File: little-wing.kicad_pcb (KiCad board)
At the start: 2 copper layers, 119.8 x 95.1 mm, 72 parts, among them IC1 AP7335-WG-7, J1 nice!view, J2 Battery, J3 trackball, J4 trackball, SW1 Power, SW2 Reset, U1 nice!nano v2, U2 PMW3610

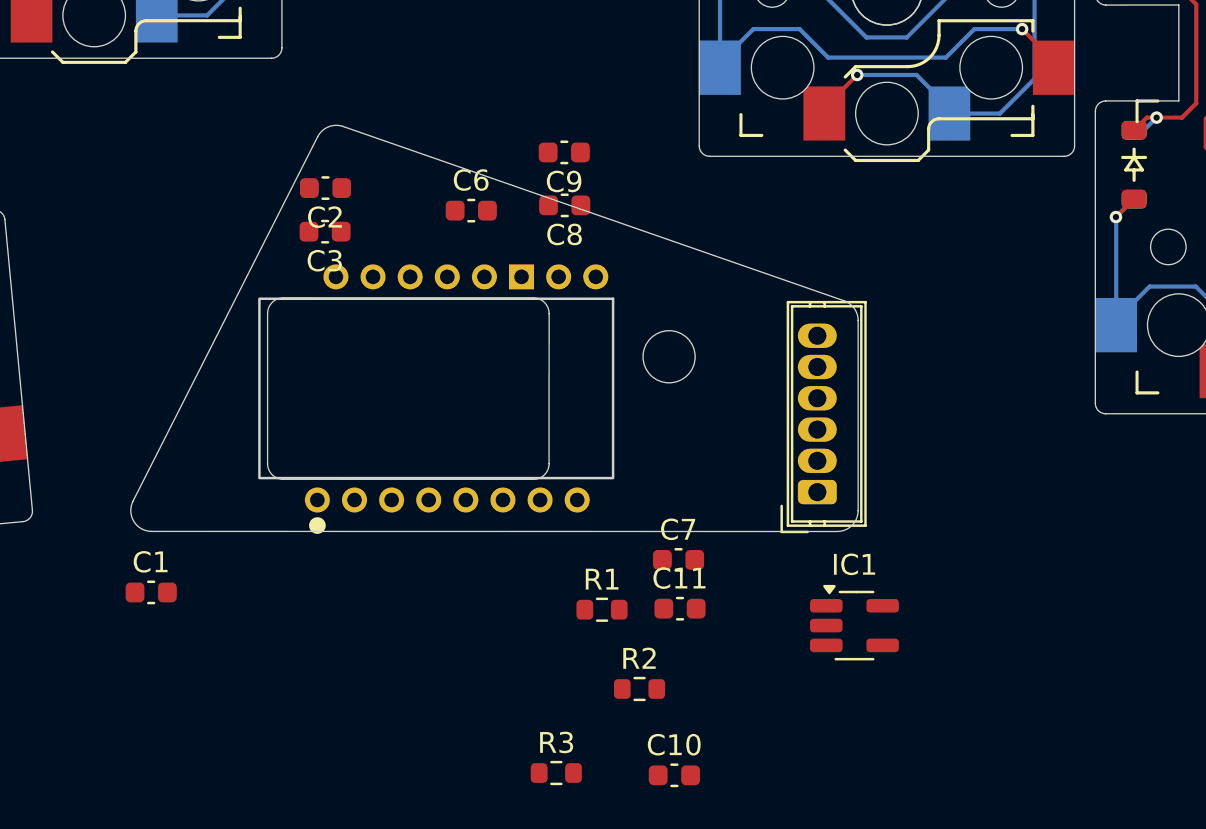
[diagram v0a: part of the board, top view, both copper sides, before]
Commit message: Initial alignment of the sensor block
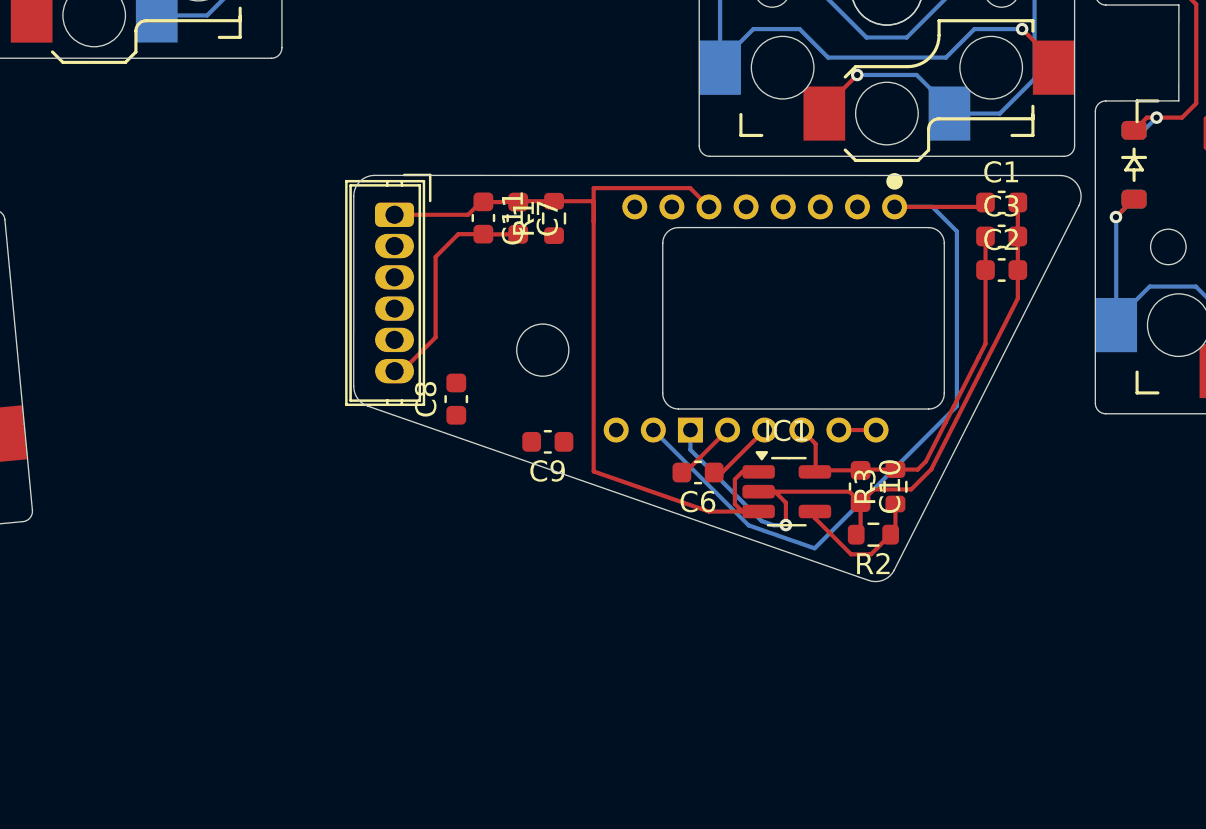
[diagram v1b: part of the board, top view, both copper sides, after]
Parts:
- moved C1 44.9 mm to (188.5, 124.5)
- moved C2 32.7 mm to (188.5, 127.7), turned to 0 degrees
- moved C3 32.4 mm to (188.5, 126.1), turned to 0 degrees
- moved J3 24.2 mm to (159.4, 125.1), turned to -90 degrees
- moved R3 21.3 mm to (183.4, 138.1), turned to 90 degrees
- moved C11 21.0 mm to (163.6, 125.2), turned to -90 degrees
- moved U2 19.4 mm to (179.1, 130.1), turned to -90 degrees
- moved R1 18.9 mm to (167.0, 125.3), turned to 90 degrees
- moved C7 18.1 mm to (165.3, 125.3), turned to -90 degrees
- moved C6 16.6 mm to (173.9, 137.4), turned to 180 degrees
- moved C10 16.5 mm to (181.7, 138.1), turned to -90 degrees
- moved C9 13.9 mm to (166.7, 136.0)
- moved R2 13.4 mm to (182.3, 140.4), turned to 180 degrees
- moved C8 10.6 mm to (162.3, 133.9), turned to 90 degrees
- moved IC1 7.19 mm to (178.2, 138.4)
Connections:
- D1 pad 1: Row 0 -> Row 2
- D10 pad 1: Row 0 -> Row 2
- D12 pad 1: Row 2 -> Row 0
- D13 pad 1: Row 0 -> Row 2
- D15 pad 1: Row 2 -> Row 0
- D16 pad 1: Row 0 -> Row 2
- D3 pad 1: Row 2 -> Row 0
- D4 pad 1: Row 0 -> Row 2
- D6 pad 1: Row 2 -> Row 0
- D7 pad 1: Row 0 -> Row 2
- D9 pad 1: Row 2 -> Row 0
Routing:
- net Row 2: track 398.2 -> 165.3 mm, vias 26 -> 6
- net Row 0: track 165.3 -> 398.2 mm, vias 6 -> 26
- net GND: track 504.3 -> 549.9 mm, vias 15 -> 16
- net 3.3v: track 0.00 -> 42.3 mm
- net Net-(U2-+VCSEL): track 0.00 -> 35.8 mm
- net +1V9: track 0.00 -> 19.7 mm
- net Net-(IC1-ADJ): track 0.00 -> 6.62 mm
- net Net-(U2-CN): track 0.00 -> 3.26 mm
- net Net-(U2-CP): track 0.00 -> 3.03 mm
- net Net-(U2--VCSEL): track 0.00 -> 1.78 mm
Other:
- outline, holes or cut-outs redrawn

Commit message: Wiring togother the sensor board
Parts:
- moved C1 40.6 mm to (150.5, 139.0), turned to 180 degrees
- moved C3 39.6 mm to (150.5, 137.3), turned to 180 degrees
- moved C2 38.8 mm to (150.5, 135.7), turned to 180 degrees
- moved R2 30.8 mm to (156.9, 123.0), turned to 0 degrees
- moved R3 30.6 mm to (155.6, 125.3), turned to -90 degrees
- moved C10 27.6 mm to (157.3, 125.4), turned to 90 degrees
- moved J3 24.2 mm to (179.5, 138.4), turned to 90 degrees
- moved IC1 21.8 mm to (160.8, 125.1), turned to 180 degrees
- moved U2 19.4 mm to (159.9, 133.4), turned to 90 degrees
- moved C11 17.5 mm to (175.4, 138.2), turned to 90 degrees
- moved C7 15.5 mm to (173.7, 138.2), turned to 90 degrees
- moved C8 14.8 mm to (176.9, 136.4), turned to -90 degrees
- moved C6 14.4 mm to (165.1, 126.0), turned to 0 degrees
- moved R1 13.9 mm to (172.0, 138.2), turned to -90 degrees
- moved C9 10.6 mm to (176.9, 133.3), turned to 90 degrees
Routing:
- net SCLK: track 0.00 -> 53.9 mm, vias 0 -> 2
- net SDIO: track 0.00 -> 53.3 mm
- net NCS: track 0.00 -> 18.3 mm
- net GND: track 549.9 -> 566.8 mm
- net Net-(U2-VCP): track 0.48 -> 15.9 mm
- net MOTION: track 0.00 -> 15.1 mm
- net Net-(U2-NRESET): track 0.00 -> 6.21 mm
- net Net-(U2-+VCSEL): track 35.8 -> 31.9 mm
- net 3.3v: track 42.3 -> 41.4 mm, vias 0 -> 4
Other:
- outline, holes or cut-outs redrawn

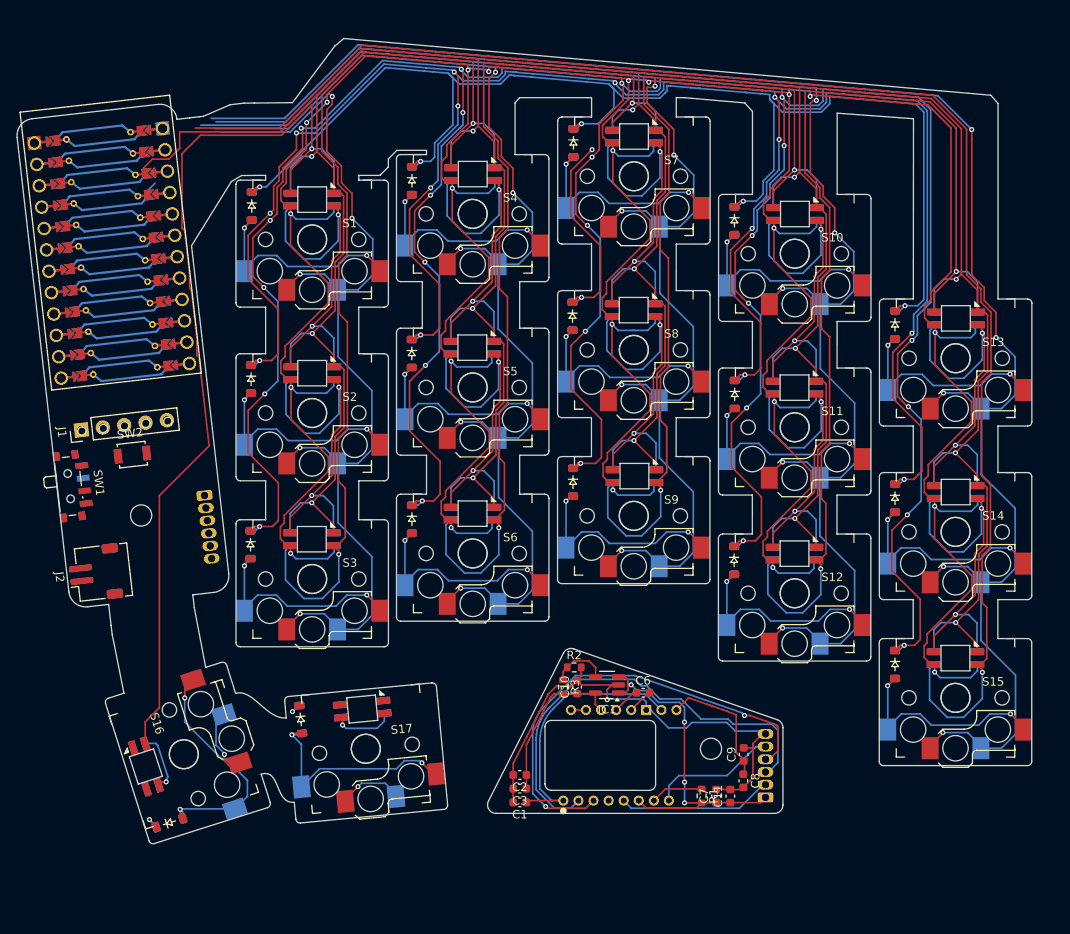
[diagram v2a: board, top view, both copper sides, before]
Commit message: Rounding out the main columns cutouts
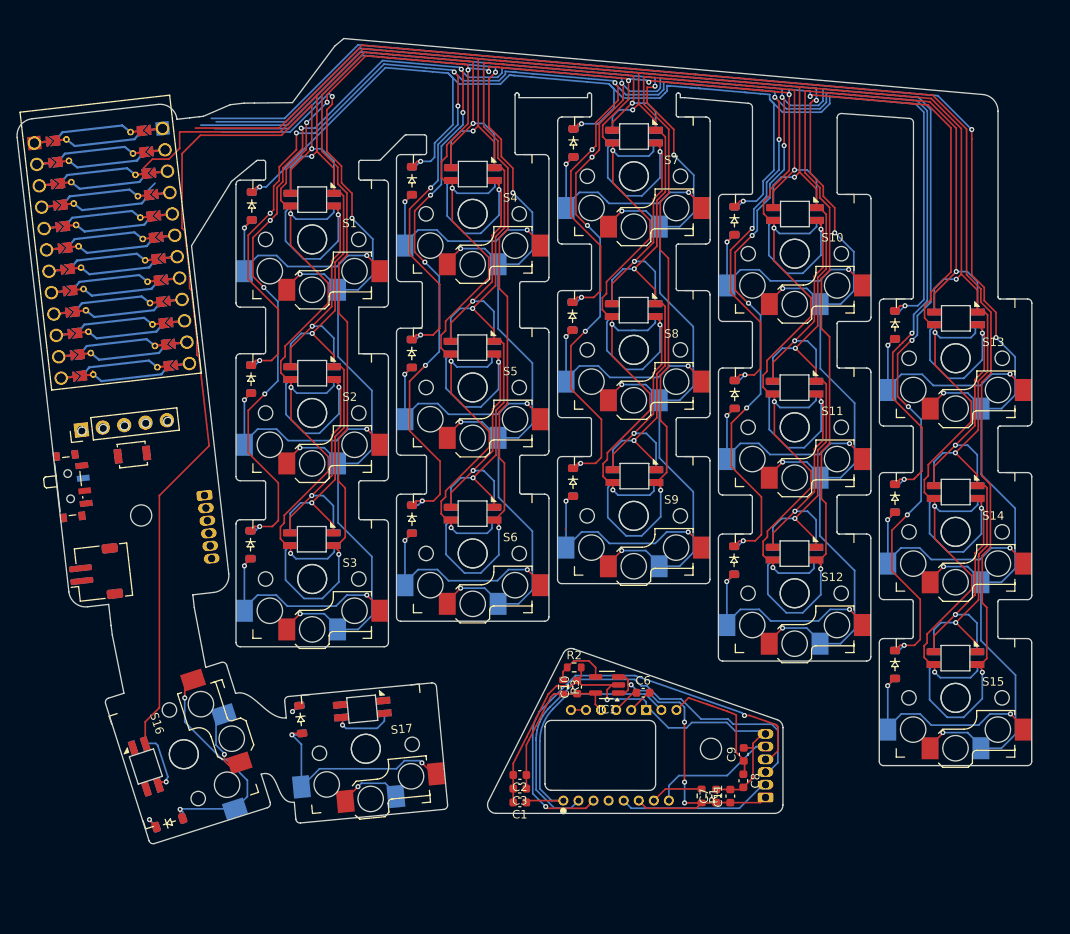
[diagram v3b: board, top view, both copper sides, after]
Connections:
- U1 pad 10: Row 0 -> Row 1
- U1 pad 11: Row 1 -> Row 2
- U1 pad 12: Row 2 -> unconnected-(U1-9-Pad12)
- U1 pad 13: Col 5 -> unconnected-(U1-10-Pad13)
- U1 pad 14: Col 4 -> unconnected-(U1-16-Pad14)
- U1 pad 15: Col 3 -> Col 5
- U1 pad 16: Col 2 -> Col 4
- U1 pad 17: Col 1 -> Col 3
- U1 pad 18: Col 0 -> Col 2
- U1 pad 19: unconnected-(U1-20-Pad19) -> Col 1
- U1 pad 20: unconnected-(U1-21-Pad20) -> Col 0
- U1 pad 5: SCK -> RGB
- U1 pad 8: RGB -> SCK
- U1 pad 9: unconnected-(U1-6-Pad9) -> Row 0
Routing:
- net Row 1: track 277.2 -> 286.5 mm
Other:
- outline, holes or cut-outs redrawn

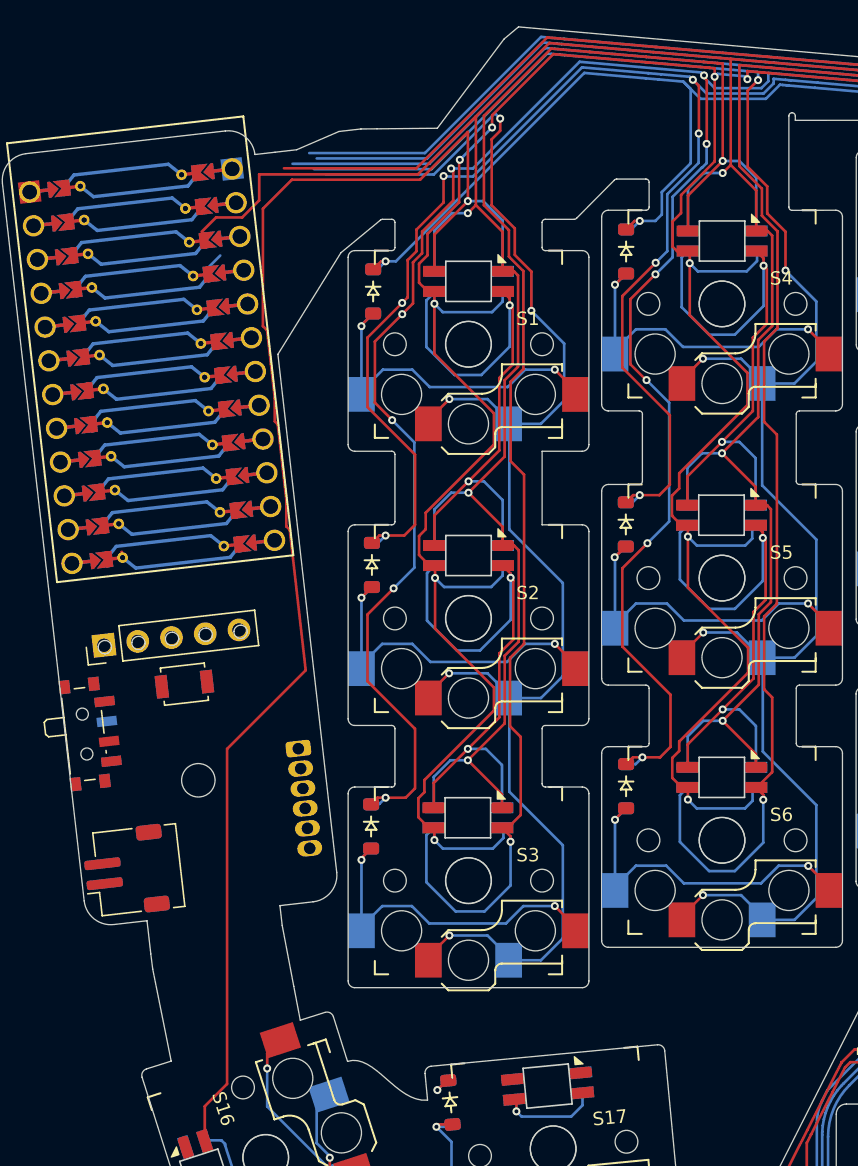
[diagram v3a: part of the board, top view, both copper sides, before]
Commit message: Refactoring the main junction a bit
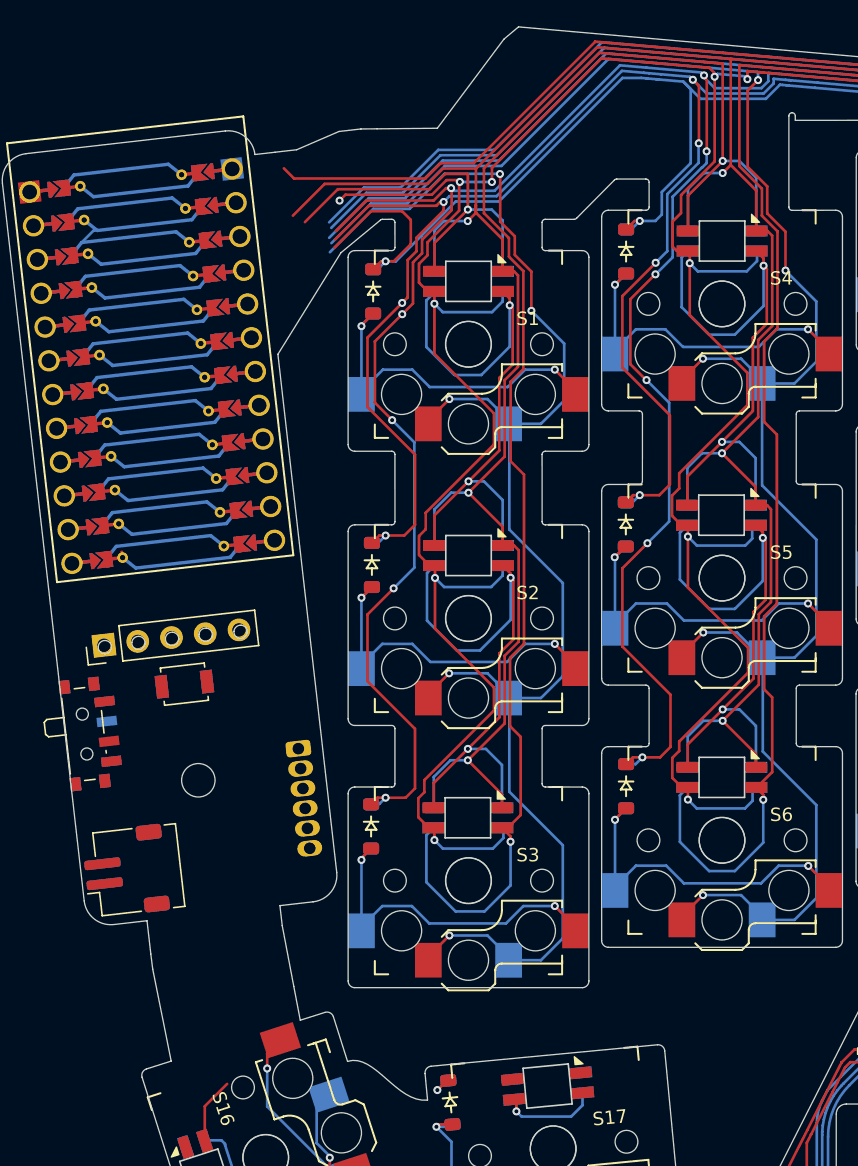
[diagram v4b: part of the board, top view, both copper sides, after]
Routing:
- net Net-(D19-DIN): track 109.5 -> 33.7 mm
- net GND: track 566.8 -> 554.6 mm
- net Row 2: track 165.3 -> 176.5 mm
- net Row 0: track 398.2 -> 407.2 mm
- net Row 1: track 286.5 -> 294.5 mm
- net VCC: track 534.3 -> 541.3 mm, vias 25 -> 26
- net Col 4: track 118.2 -> 113.5 mm
- net Net-(D22-DIN): track 114.3 -> 111.9 mm
- net (no net): track 0.00 -> 1.55 mm
- net Col 1: track 179.1 -> 180.0 mm
- net Col 3: track 138.8 -> 139.6 mm
- net Col 2: track 154.5 -> 153.8 mm
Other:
- outline, holes or cut-outs redrawn

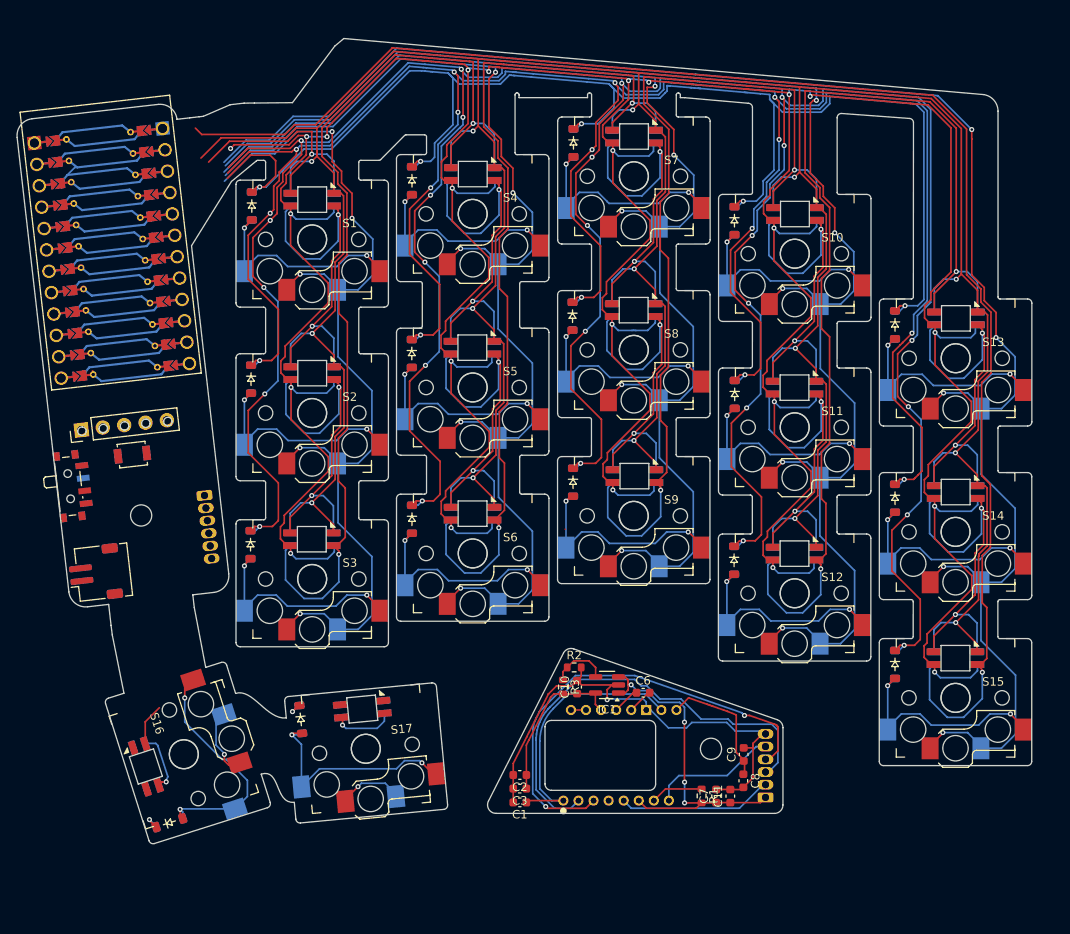
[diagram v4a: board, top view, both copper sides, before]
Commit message: Initial MCU wiring
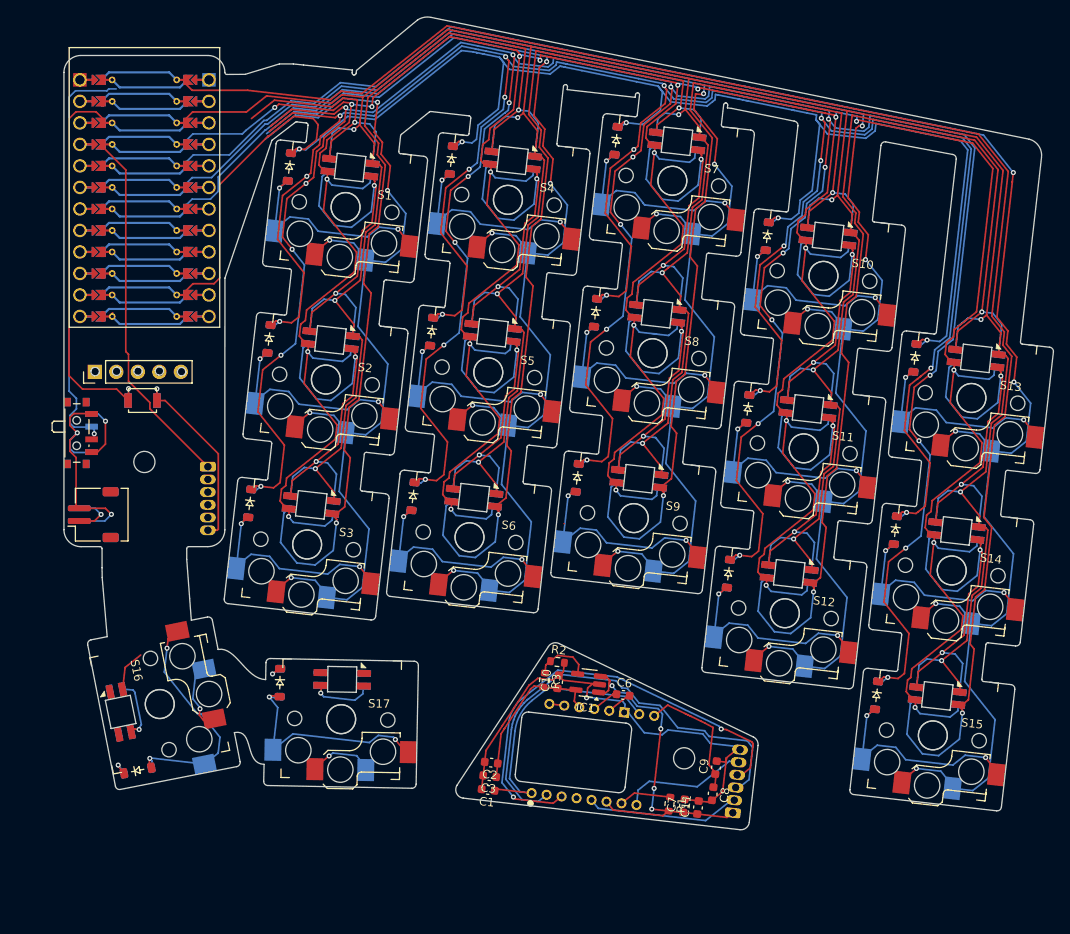
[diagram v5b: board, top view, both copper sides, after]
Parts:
- moved U1 7.56 mm to (106.2, 67.6), turned to -90 degrees
- moved D16 7.22 mm to (105.4, 135.2), turned to 11.5 degrees
- moved D19 7.10 mm to (103.4, 128.3), turned to 101.5 degrees
- moved J1 7.05 mm to (100.3, 88.1), turned to 90 degrees
- moved J2 6.90 mm to (100.1, 105.0), turned to 90 degrees
- moved S16 6.57 mm to (108.0, 127.4), turned to 101.5 degrees
- moved SW2 6.50 mm to (106.0, 91.5), turned to 180 degrees
- moved D1 6.39 mm to (123.3, 63.9), turned to -96.5 degrees
- moved SW1 6.31 mm to (98.5, 95.4), turned to -90 degrees
- moved D20 5.86 mm to (130.5, 64.0), turned to -6.5 degrees
- moved S1 5.49 mm to (129.9, 68.7), turned to -6.5 degrees
- moved D32 5.30 mm to (204.4, 86.5), turned to -6.5 degrees
- moved D4 5.25 mm to (142.4, 63.1), turned to -96.5 degrees
- moved D2 5.20 mm to (120.9, 84.3), turned to -96.5 degrees
- moved S15 5.18 mm to (199.3, 131.1), turned to -6.5 degrees
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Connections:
- U1 pad 1: CS_D -> RGB
- U1 pad 2: CS_T -> SCK
- U1 pad 5: RGB -> MOSI
- U1 pad 6: MOSI -> MISO
- U1 pad 7: MISO -> CS_T
- U1 pad 8: SCK -> CS_D
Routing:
- net VCC: track 541.3 -> 596.4 mm
- net BAT: track 0.00 -> 49.8 mm, vias 0 -> 1
- net RESET: track 0.00 -> 46.2 mm, vias 0 -> 1
- net GND: track 554.6 -> 590.5 mm, vias 16 -> 18
- net Net-(J2-Pin_2): track 0.00 -> 27.9 mm, vias 0 -> 2
- net Row 2: track 176.5 -> 200.5 mm
- net Col 2: track 153.8 -> 168.2 mm
- net Col 1: track 180.0 -> 192.9 mm
- net Col 0: track 208.3 -> 220.3 mm
- net RGB: track 180.8 -> 187.5 mm
- net (no net): track 1.55 -> 6.73 mm, vias 0 -> 1
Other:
- board size 119.8 x 95.1 mm -> 116.8 x 96 mm
